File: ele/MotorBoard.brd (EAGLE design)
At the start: 20 x 16 mm, 19 parts

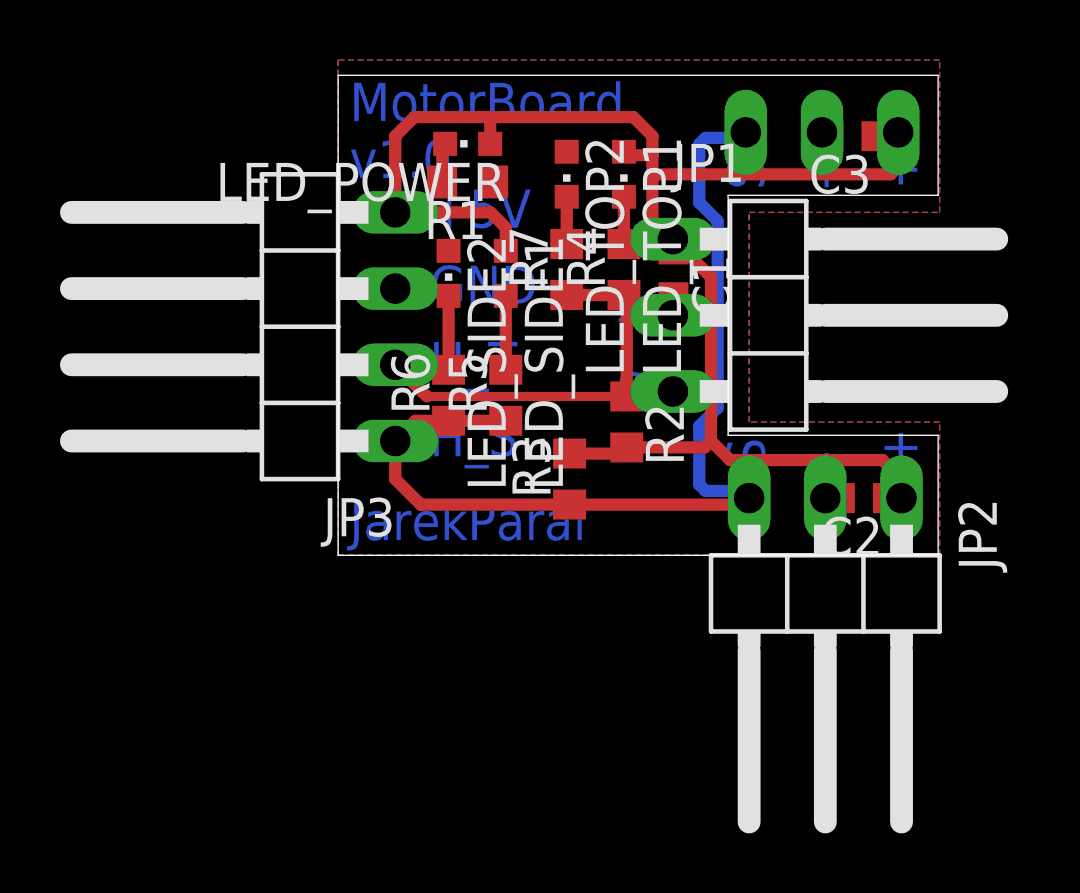
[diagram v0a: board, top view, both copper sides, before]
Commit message: ele: MotorBoard - fix the bug with the LEDs
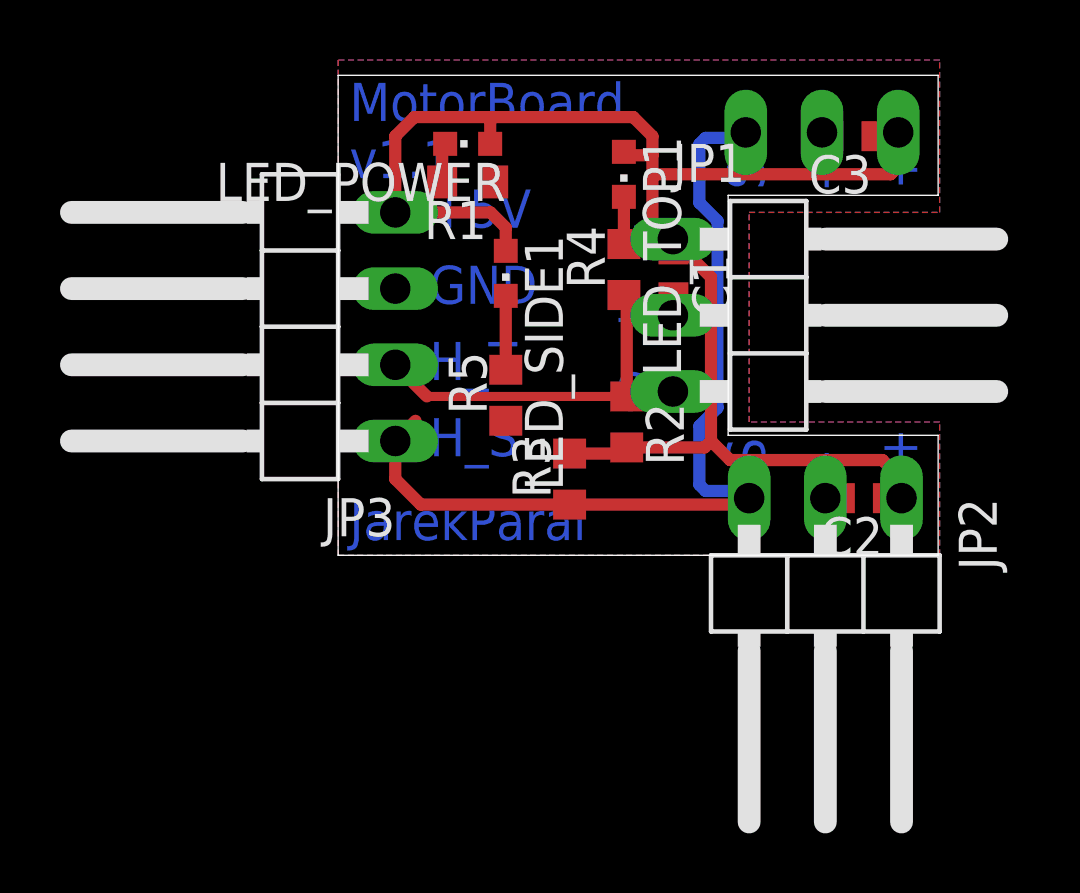
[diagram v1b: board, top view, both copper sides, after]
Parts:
- removed LED_SIDE2, LED_TOP2: red, led:CHIPLED_0603
- removed R6, R7: 1k, rcl:R0603
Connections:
- removed net LED_SIDE2: LED_SIDE2.C, R6.2
- removed net LED_TOP2: LED_TOP2.C, R7.2
- net GND: no longer LED_SIDE2.A, LED_TOP2.A
- net HAL_SIDE: no longer R6.1
- net HAL_TOP: no longer R7.1
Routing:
- net HAL_SIDE: track 32.9 -> 29.9 mm
- net LED_SIDE2: track 2.46 -> 0.00 mm
- net HAL_TOP: track 15.4 -> 13.5 mm
- net LED_TOP2: track 1.57 -> 0.00 mm
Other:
- board text added: "MotorBoard v1.1"
- board text added: "v1.1"
- board text removed: "MotorBoard v1.0"
- board text removed: "v1.0"
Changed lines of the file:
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@@
 <layer number="49" name="Reference" color="7" fill="1" visible="no" active="yes"/>
 <layer number="50" name="dxf" color="7" fill="1" visible="no" active="no"/>
-<layer number="51" name="tDocu" color="7" fill="1" visible="no" active="yes"/>
-<layer number="52" name="bDocu" color="7" fill="1" visible="no" active="yes"/>
+<layer number="51" name="tDocu" color="7" fill="1" visible="yes" active="yes"/>
+<layer number="52" name="bDocu" color="7" fill="1" visible="yes" active="yes"/>
 <layer number="53" name="tGND_GNDA" color="7" fill="9" visible="no" active="no"/>
 <layer number="54" name="bGND_GNDA" color="1" fill="9" visible="no" active="no"/>
@@
 <text x="19.304" y="2.921" size="1.27" layer="16" font="vector" ratio="20" rot="R90">+</text>
 <text x="0.381" y="12.573" size="1.27" layer="16" font="vector" ratio="20">MotorBoard
-v1.0</text>
+v1.1</text>
 <text x="0.381" y="0.508" size="1.27" layer="16" font="vector" ratio="20">JarekParal</text>
-<text x="10.16" y="14.478" size="1.016" layer="51" font="vector" ratio="20">v1.0</text>
+<text x="10.16" y="14.478" size="1.016" layer="51" font="vector" ratio="20">v1.1</text>
 <text x="14.224" y="12.192" size="1.27" layer="16" font="vector" ratio="20" rot="R90">S</text>
 <text x="16.764" y="12.192" size="1.27" layer="16" font="vector" ratio="20" rot="R90">-</text>
@@
 <attribute name="RS" value="872-1799" x="11.303" y="0.508" size="1.778" layer="27" rot="R180" display="off"/>
 </element>
-<element name="R6" library="rcl" library_urn="urn:adsk.eagle:library:334" package="R0603" package3d_urn="urn:adsk.eagle:package:23555/2" value="1k" x="3.683" y="5.334" rot="R90">
-<attribute name="SPICEPREFIX" value="R" x="-6.477" y="5.334" size="1.778" layer="27" rot="R90" display="off"/>
-</element>
-<element name="LED_SIDE2" library="led" package="CHIPLED_0603" value="red" x="3.683" y="9.398" rot="R180">
-<attribute name="DIGIKEY" value="160-1446-1-ND" x="9.398" y="4.318" size="1.778" layer="27" rot="R180" display="off"/>
-<attribute name="FARNELL" value="2293494" x="9.398" y="4.318" size="1.778" layer="27" rot="R180" display="off"/>
-<attribute name="MOUSER" value="859-LTST-C191KGKT" x="9.398" y="4.318" size="1.778" layer="27" rot="R180" display="off"/>
-<attribute name="RS" value="872-1799" x="9.398" y="4.318" size="1.778" layer="27" rot="R180" display="off"/>
-</element>
-<element name="R7" library="rcl" library_urn="urn:adsk.eagle:library:334" package="R0603" package3d_urn="urn:adsk.eagle:package:23555/2" value="1k" x="7.62" y="9.525" rot="R90">
-<attribute name="SPICEPREFIX" value="R" x="-1.905" y="9.525" size="1.778" layer="27" rot="R90" display="off"/>
-</element>
-<element name="LED_TOP2" library="led" package="CHIPLED_0603" value="red" x="7.62" y="12.7" rot="R180">
-<attribute name="DIGIKEY" value="160-1446-1-ND" x="13.335" y="8.255" size="1.778" layer="27" rot="R180" display="off"/>
-<attribute name="FARNELL" value="2293494" x="13.335" y="8.255" size="1.778" layer="27" rot="R180" display="off"/>
-<attribute name="MOUSER" value="859-LTST-C191KGKT" x="13.335" y="8.255" size="1.778" layer="27" rot="R180" display="off"/>
-<attribute name="RS" value="872-1799" x="13.335" y="8.255" size="1.778" layer="27" rot="R180" display="off"/>
-</element>
 <element name="C1" library="rcl" library_urn="urn:adsk.eagle:library:334" package="C0603" package3d_urn="urn:adsk.eagle:package:23616/2" value="100n/6,3V" x="11.176" y="9.398" rot="R270">
 <attribute name="SPICEPREFIX" value="C" x="11.176" y="9.398" size="1.778" layer="27" rot="R270" display="off"/>
@@
 <vertex x="0" y="16.51"/>
 </polygon>
-<contactref element="LED_TOP2" pad="A"/>
-<contactref element="LED_SIDE2" pad="A"/>
 <contactref element="C1" pad="2"/>
 <contactref element="C2" pad="2"/>
@@
 <wire x1="9.62" y1="5.295" x2="2.96" y2="5.295" width="0.3048" layer="1"/>
 <wire x1="2.96" y1="5.295" x2="1.905" y2="6.35" width="0.4064" layer="1"/>
-<contactref element="R7" pad="1"/>
 <wire x1="9.62" y1="5.295" x2="9.62" y2="8.255" width="0.4064" layer="1"/>
 <wire x1="9.62" y1="8.255" x2="9.62" y2="8.58" width="0.4064" layer="1"/>
-<wire x1="7.62" y1="8.675" x2="9.525" y2="8.675" width="0.4064" layer="1"/>
 <wire x1="9.525" y1="8.675" x2="9.525" y2="8.35" width="0.1524" layer="1"/>
 <wire x1="9.525" y1="8.35" x2="9.62" y2="8.255" width="0.1524" layer="1"/>
@@
 <contactref element="R5" pad="2"/>
 <wire x1="5.588" y1="6.184" x2="5.588" y2="8.648" width="0.4064" layer="1"/>
-</signal>
-<signal name="LED_SIDE2">
-<contactref element="LED_SIDE2" pad="C"/>
-<contactref element="R6" pad="2"/>
-<wire x1="3.683" y1="6.184" x2="3.683" y2="8.648" width="0.4064" layer="1"/>
-</signal>
-<signal name="LED_TOP2">
-<contactref element="LED_TOP2" pad="C"/>
-<contactref element="R7" pad="2"/>
-<wire x1="7.62" y1="10.375" x2="7.62" y2="11.95" width="0.4064" layer="1"/>
 </signal>
 <signal name="HAL_SIDE">
@@
 <contactref element="JP2" pad="3"/>
 <contactref element="R3" pad="1"/>
-<contactref element="R6" pad="1"/>
 <wire x1="13.7" y1="1.905" x2="13.485" y2="1.69" width="0.4064" layer="1"/>
 <wire x1="13.485" y1="1.69" x2="7.715" y2="1.69" width="0.4064" layer="1"/>
 <wire x1="2.755" y1="1.69" x2="1.905" y2="2.54" width="0.4064" layer="1"/>
 <wire x1="1.905" y1="2.54" x2="1.905" y2="3.81" width="0.4064" layer="1"/>
-<wire x1="5.588" y1="4.484" x2="3.683" y2="4.484" width="0.4064" layer="1"/>
-<wire x1="3.683" y1="4.484" x2="2.579" y2="4.484" width="0.4064" layer="1"/>
 <wire x1="2.579" y1="4.484" x2="1.905" y2="3.81" width="0.4064" layer="1"/>
 <wire x1="7.715" y1="1.69" x2="2.755" y2="1.69" width="0.4064" layer="1"/>
@@
 <wire x1="12.6468" y1="11.14456875" x2="12.6468" y2="4.913875" width="0.4064" layer="16"/>
 <wire x1="12.6468" y1="4.913875" x2="12.042" y2="4.309075" width="0.4064" layer="16"/>
+<wire x1="2.579" y1="4.484" x2="5.588" y2="4.484" width="0" layer="19" extent="1-1"/>
 </signal>
 </signals>
